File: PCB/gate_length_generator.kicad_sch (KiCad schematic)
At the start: 12 parts

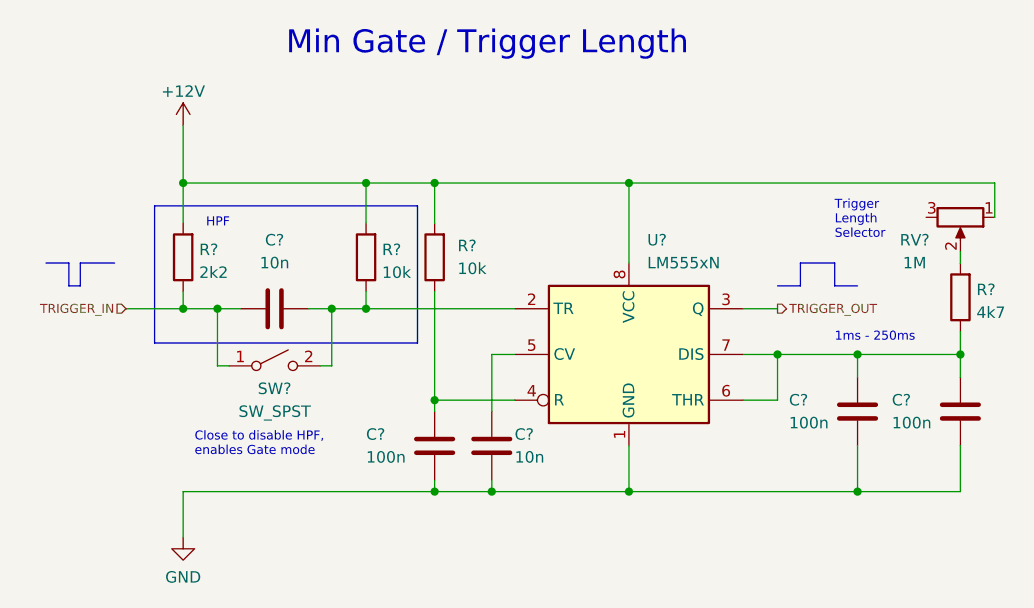
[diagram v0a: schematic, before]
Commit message: :wrench: Set footprint for gate/trigger switch
Change the symbol to match the chosen footprint and set the footprint.

Fixes: #22
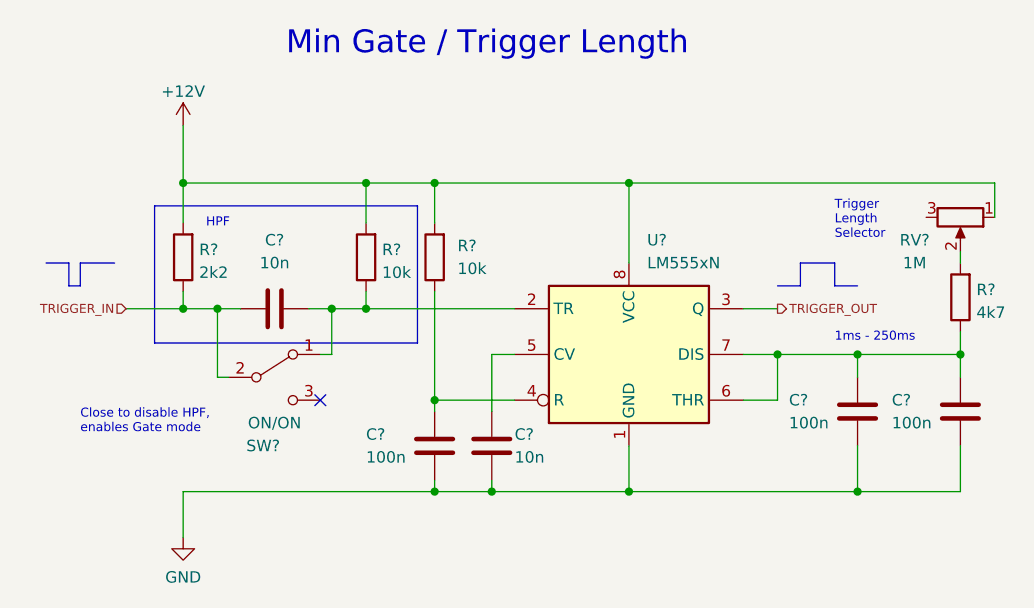
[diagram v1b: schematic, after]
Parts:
- removed SW?: SW_SPST, symbol Switch:SW_SPST
- added SW?: ON/ON, mopsy:Switch_SPDT_TSM103A2_Befaco, symbol Switch:SW_SPDT
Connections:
- net TRIGGER_IN: now also SW?.2 (B)
- net at C?.2, R?.1, U?.2 (TR): now also SW?.1 (A)
- no-connect marks 0 -> 1
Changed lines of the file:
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@@
   (junction (at 60.96 53.34) (diameter 0) (color 0 0 0 0)
   )
+  (no_connect (at 55.88 63.5))
   (wire (pts (xy 60.96 53.34) (xy 77.47 53.34))
     (stroke (width 0) (type default) (color 0 0 0 0))
@@
     (stroke (width 0) (type default) (color 0 0 0 0))
   )
-  (wire (pts (xy 45.72 59.69) (xy 44.45 59.69))
+  (wire (pts (xy 45.72 60.96) (xy 44.45 60.96))
     (stroke (width 0) (type default) (color 0 0 0 0))
   )
@@
     (stroke (width 0) (type default) (color 0 0 0 0))
   )
-  (wire (pts (xy 55.88 59.69) (xy 57.15 59.69))
+  (wire (pts (xy 55.88 58.42) (xy 57.15 58.42))
     (stroke (width 0) (type default) (color 0 0 0 0))
   )
@@
     (stroke (width 0) (type default) (color 0 0 0 0))
   )
-  (wire (pts (xy 57.15 53.34) (xy 57.15 59.69))
+  (wire (pts (xy 57.15 53.34) (xy 57.15 58.42))
     (stroke (width 0) (type default) (color 0 0 0 0))
   )
@@
     (stroke (width 0) (type default) (color 0 0 0 0))
   )
-  (wire (pts (xy 44.45 53.34) (xy 44.45 59.69))
+  (wire (pts (xy 44.45 53.34) (xy 44.45 60.96))
     (stroke (width 0) (type default) (color 0 0 0 0))
   )
@@
     (effects (font (size 1 1)) (justify left bottom))
   )
-  (text "Close to disable HPF,\nenables Gate mode" (at 41.91 69.85 0)
+  (text "Close to disable HPF,\nenables Gate mode" (at 29.21 67.31 0)
     (effects (font (size 1 1)) (justify left bottom))
   )
@@
     (pin "2")
   )
-  (symbol (lib_id "Switch:SW_SPST") (at 50.8 59.69 0) (unit 1)
-    (in_bom yes) (on_board yes)
-    (property "Reference" "SW?" (id 0) (at 50.8 62.23 0))
-    (property "Value" "SW_SPST" (id 1) (at 50.8 64.77 0))
-    (property "Footprint" "" (id 2) (at 50.8 59.69 0)
-      (effects (font (size 1.27 1.27)) hide)
-    )
-    (property "Datasheet" "~" (id 3) (at 50.8 59.69 0)
-      (effects (font (size 1.27 1.27)) hide)
-    )
-    (pin "1")
-    (pin "2")
-  )
   (symbol (lib_id "Device:R") (at 127 52.07 180) (unit 1)
     (in_bom yes) (on_board yes) (fields_autoplaced)
@@
     (pin "2")
   )
+  (symbol (lib_id "Switch:SW_SPDT") (at 50.8 60.96 0) (unit 1)
+    (in_bom yes) (on_board yes)
+    (property "Reference" "SW?" (id 0) (at 49.53 68.58 0))
+    (property "Value" "ON/ON" (id 1) (at 50.8 66.04 0))
+    (property "Footprint" "mopsy:Switch_SPDT_TSM103A2_Befaco" (id 2) (at 50.8 60.96 0)
+      (effects (font (size 1.27 1.27)) hide)
+    )
+    (property "Datasheet" "~" (id 3) (at 50.8 60.96 0)
+      (effects (font (size 1.27 1.27)) hide)
+    )
+    (pin "1")
+    (pin "2")
+    (pin "3")
+  )
   (symbol (lib_id "Timer:LM555xN") (at 90.17 58.42 0) (unit 1)

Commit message: :wrench: Assign a potentiometer footprint
Assign footprint for https://shop.befaco.org/potentiometers/279-5x-potentiometer-1m.html
from the moPsy resources.

Fixes: #17
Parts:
- RV?: footprint (none) -> mopsy:Potentiometer_Befaco_12mm_Single_Vertical
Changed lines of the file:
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@@
     (property "Reference" "RV?" (id 0) (at 121.92 45.72 90))
     (property "Value" "1M" (id 1) (at 121.92 48.26 90))
-    (property "Footprint" "" (id 2) (at 127 43.18 0)
+    (property "Footprint" "mopsy:Potentiometer_Befaco_12mm_Single_Vertical" (id 2) (at 127 43.18 0)
       (effects (font (size 1.27 1.27)) hide)
     )

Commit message: :hammer: Change voltage switch footprint and move KiCad version
Unfortunately KiCad did all in one move, so this is a compound commit.

Fixes #6
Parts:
- SW?: footprint mopsy:Switch_SPDT_TSM103A2_Befaco -> moPsy:PB_Hor_7x7_2pole

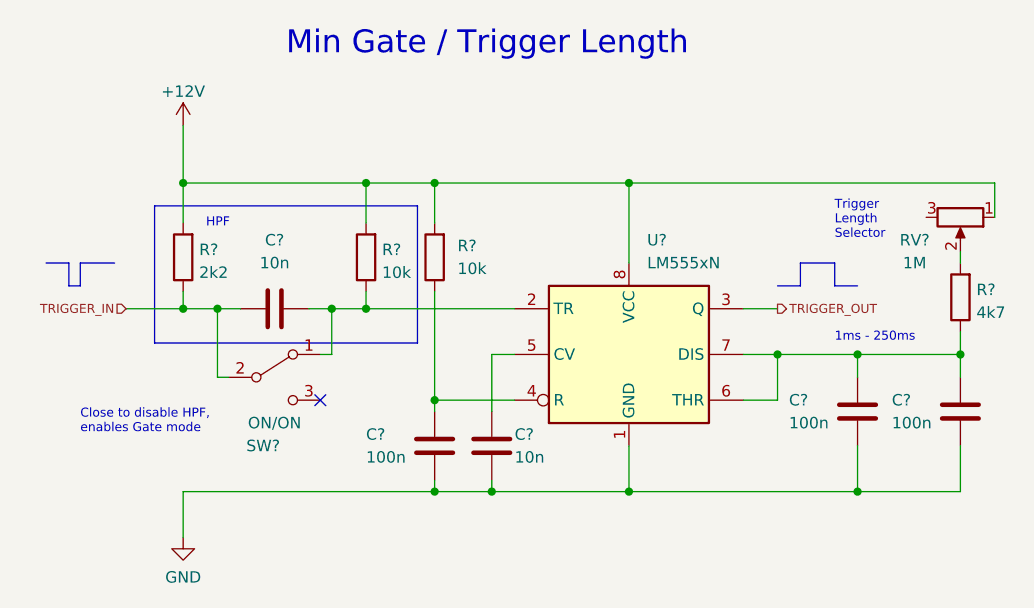
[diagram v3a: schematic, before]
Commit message: :wrench: Assign component designators
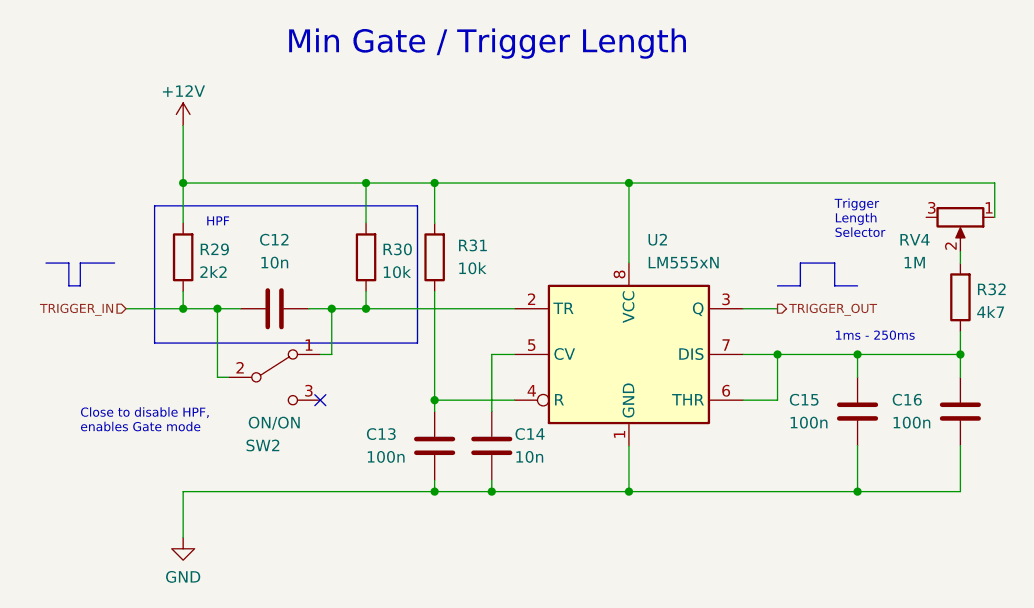
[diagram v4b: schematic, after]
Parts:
- gave numbers to parts that had none: 12

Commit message: :wrench: Assign footprints to all symbols
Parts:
- C12, C13, C14, C15, C16: footprint (none) -> Capacitor_THT:C_Disc_D4.3mm_W1.9mm_P5.00mm
- R29, R30, R31, R32: footprint (none) -> Resistor_THT:R_Axial_DIN0207_L6.3mm_D2.5mm_P7.62mm_Horizontal
- RV4: footprint mopsy:Potentiometer_Befaco_12mm_Single_Vertical -> moPsy:Potentiometer_Befaco_12mm_Single_Vertical
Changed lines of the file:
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@@
       (effects (font (size 1.27 1.27)) (justify left))
     )
-    (property "Footprint" "" (at 75.8952 72.39 0)
+    (property "Footprint" "Capacitor_THT:C_Disc_D4.3mm_W1.9mm_P5.00mm" (at 75.8952 72.39 0)
       (effects (font (size 1.27 1.27)) hide)
     )
@@
       (effects (font (size 1.27 1.27)) (justify right))
     )
-    (property "Footprint" "" (at 62.738 47.625 90)
+    (property "Footprint" "Resistor_THT:R_Axial_DIN0207_L6.3mm_D2.5mm_P7.62mm_Horizontal" (at 62.738 47.625 90)
       (effects (font (size 1.27 1.27)) hide)
     )
@@
       (effects (font (size 1.27 1.27)))
     )
-    (property "Footprint" "mopsy:Potentiometer_Befaco_12mm_Single_Vertical" (at 127 43.18 0)
+    (property "Footprint" "moPsy:Potentiometer_Befaco_12mm_Single_Vertical" (at 127 43.18 0)
       (effects (font (size 1.27 1.27)) hide)
     )
@@
       (effects (font (size 1.27 1.27)) (justify left))
     )
-    (property "Footprint" "" (at 69.5452 72.39 0)
+    (property "Footprint" "Capacitor_THT:C_Disc_D4.3mm_W1.9mm_P5.00mm" (at 69.5452 72.39 0)
       (effects (font (size 1.27 1.27)) hide)
     )
@@
       (effects (font (size 1.27 1.27)))
     )
-    (property "Footprint" "" (at 54.61 52.3748 0)
+    (property "Footprint" "Capacitor_THT:C_Disc_D4.3mm_W1.9mm_P5.00mm" (at 54.61 52.3748 0)
       (effects (font (size 1.27 1.27)) hide)
     )
@@
       (effects (font (size 1.27 1.27)) (justify left))
     )
-    (property "Footprint" "" (at 127.9652 68.58 0)
+    (property "Footprint" "Capacitor_THT:C_Disc_D4.3mm_W1.9mm_P5.00mm" (at 127.9652 68.58 0)
       (effects (font (size 1.27 1.27)) hide)
     )
@@
       (effects (font (size 1.27 1.27)) (justify right))
     )
-    (property "Footprint" "" (at 128.778 52.07 90)
+    (property "Footprint" "Resistor_THT:R_Axial_DIN0207_L6.3mm_D2.5mm_P7.62mm_Horizontal" (at 128.778 52.07 90)
       (effects (font (size 1.27 1.27)) hide)
     )
@@
       (effects (font (size 1.27 1.27)) (justify right))
     )
-    (property "Footprint" "" (at 42.418 47.625 90)
+    (property "Footprint" "Resistor_THT:R_Axial_DIN0207_L6.3mm_D2.5mm_P7.62mm_Horizontal" (at 42.418 47.625 90)
       (effects (font (size 1.27 1.27)) hide)
     )
@@
       (effects (font (size 1.27 1.27)) (justify left))
     )
-    (property "Footprint" "" (at 116.5352 68.58 0)
+    (property "Footprint" "Capacitor_THT:C_Disc_D4.3mm_W1.9mm_P5.00mm" (at 116.5352 68.58 0)
       (effects (font (size 1.27 1.27)) hide)
     )
@@
       (effects (font (size 1.27 1.27)) (justify right))
     )
-    (property "Footprint" "" (at 70.358 47.625 90)
-      (effects (font (size 1.27 1.27)) hide)
-    )
+    (property "Footprint" "Resistor_THT:R_Axial_DIN0207_L6.3mm_D2.5mm_P7.62mm_Horizontal" (at 70.358 47.625 90)
+      (effects (font (size 1.27 1.27)) hide)
+    )

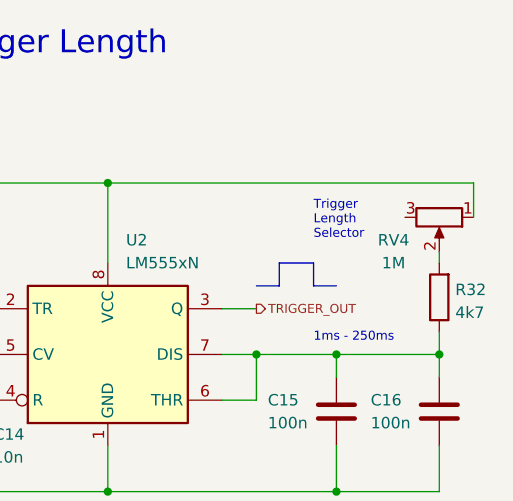
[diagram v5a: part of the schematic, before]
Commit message: :sparkles: Add PCB layout for the module
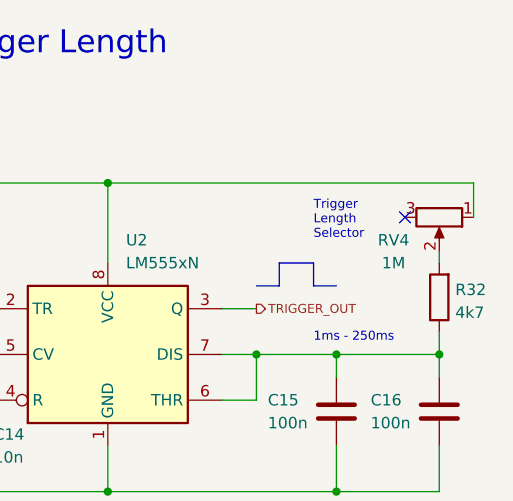
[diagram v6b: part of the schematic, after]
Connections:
- no-connect marks 1 -> 2
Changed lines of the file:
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@@
   )
   (no_connect (at 55.88 63.5))
+  (no_connect (at 123.19 43.18))
   (wire (pts (xy 60.96 53.34) (xy 77.47 53.34))
     (stroke (width 0) (type default))

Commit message: :hammer: Change switch footprints to hybrid version
This allows more flexibility when sourcing the switches

Fixes: #43
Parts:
- SW2: footprint moPsy:PB_Hor_7x7_2pole -> moPsy:PB_Hor_7x7_2pole_hybrid
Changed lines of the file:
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@@
       (effects (font (size 1.27 1.27)))
     )
-    (property "Footprint" "moPsy:PB_Hor_7x7_2pole" (at 50.8 60.96 0)
+    (property "Footprint" "moPsy:PB_Hor_7x7_2pole_hybrid" (at 50.8 60.96 0)
       (effects (font (size 1.27 1.27)) hide)
     )
